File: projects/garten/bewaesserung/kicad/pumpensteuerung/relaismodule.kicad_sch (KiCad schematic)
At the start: 5 parts, among them J1 Screw_Terminal_01x03, K2 SANYOU_SRD_Form_C, Q1 2N3904

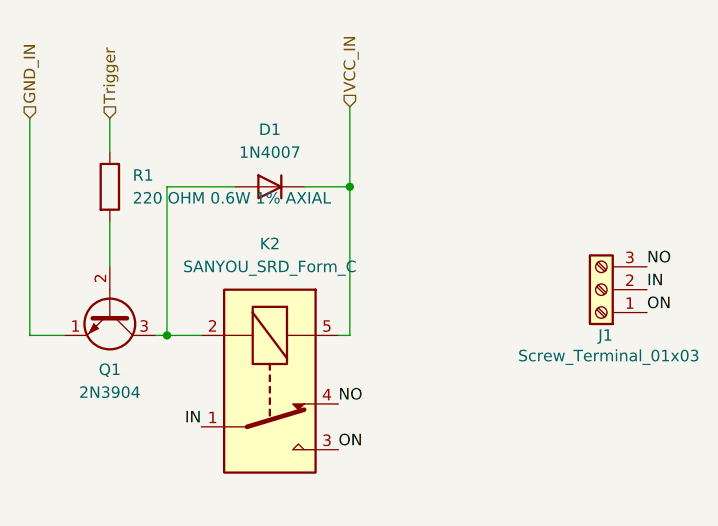
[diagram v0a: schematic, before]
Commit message: [garten/bewaesserung] change powersupply from 230VAC to 24VDC
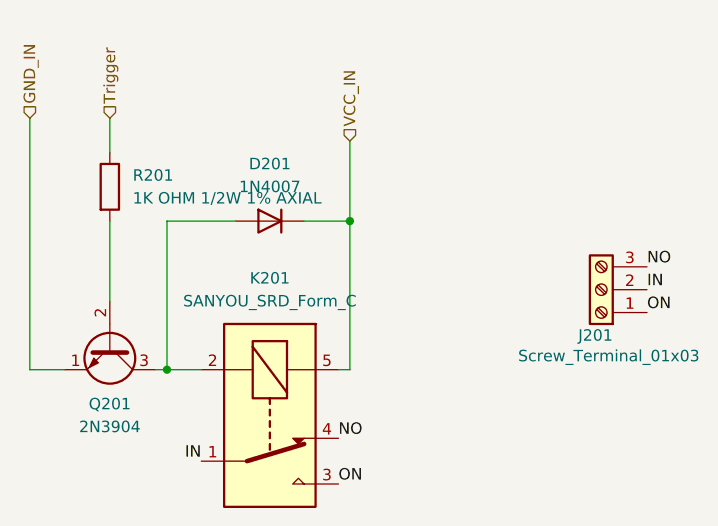
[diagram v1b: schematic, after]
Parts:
- R201: renamed from R1; value 220 OHM 0.6W 1% AXIAL -> 1K OHM 1/2W 1% AXIAL; MPN MBB02070C2200FCT00 -> SFR25H0001001FA500
- renumbered D1 to D201, J1 to J201, K2 to K201, Q1 to Q201
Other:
- title: (none) -> Pumpensteuerung
- moved on the sheet: D201, K201, Q201
